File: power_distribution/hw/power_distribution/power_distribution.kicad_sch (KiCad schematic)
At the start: 52 parts, among them J1 XT30-M_Ver, J2 JST-PH_01x02, J3 JST-PH_01x02, J4 JST-PH_01x02, Q1 60Vds, U1 LMR51635XFDDCR, U2 AP63205WU-7, U3 AP63203WU-7

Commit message: First PCB draft
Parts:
- added C24: 0.1uF, Capacitor_SMD:C_0603_1608Metric_Pad1.08x0.95mm_HandSolder, symbol Device:C
- added D9: 3.3Vrwm, ESD5Z5.0T1G:SOD-523_0P9X1P3_ONS, symbol SMBJ51A-13-F:SMBJ51A-13-F
- added F5, F6: 0.5A 16V, 0ZCH0050FF2G:0ZCH_BEL, symbol Device:Polyfuse
- added J5: JST-PH_01x02, Connector_JST:JST_PH_S2B-PH-K_1x02_P2.00mm_Horizontal, symbol Connector_Generic:Conn_01x02
- added R7: 100k, Resistor_SMD:R_0603_1608Metric_Pad0.98x0.95mm_HandSolder, symbol Device:R_US
- C3: footprint Capacitor_SMD:CP_Elec_10x10 -> Capacitor_SMD:CP_Elec_8x10
- C5: footprint Capacitor_SMD:CP_Elec_10x10 -> Capacitor_SMD:CP_Elec_6.3x7.7
- C7: footprint Capacitor_SMD:CP_Elec_10x10 -> Capacitor_SMD:CP_Elec_5x5.3
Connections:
- net GND: now also C24.2, D9.2, J5.1 (Pin_1)
- net VBAT: now also R7.2; no longer U1.2 (EN)
- net at C8.1, D7.1, J4.2 (Pin_2): now also F5.1; no longer C7.1, D8.2 (A), F4.1
- new net: C24.1, D9.1, F6.1, J5.2 (Pin_2)
- new net: R7.1, U1.2 (EN)
- new net 3V3_SPLIT: C7.1, D8.2 (A), F4.1, F5.2, F6.2
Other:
- moved on the sheet: C1, C10, C11, C12, C13, C14, C15, C16, C17, C18, C19, C2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

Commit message: Add test points
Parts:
- added 12V: 12V, TestPoint:TestPoint_Pad_D1.0mm, symbol Connector:TestPoint
- added 3V3: 3V3, TestPoint:TestPoint_Pad_D1.0mm, symbol Connector:TestPoint
- added 5V: 5V, TestPoint:TestPoint_Pad_D1.0mm, symbol Connector:TestPoint
- added EN_12V: EN_12V, TestPoint:TestPoint_Pad_D1.0mm, symbol Connector:TestPoint
- added EN_3V3: EN_3V3, TestPoint:TestPoint_Pad_D1.0mm, symbol Connector:TestPoint
- added EN_5V: EN_5V, TestPoint:TestPoint_Pad_D1.0mm, symbol Connector:TestPoint
- added FB_12V: FB_12V, TestPoint:TestPoint_Pad_D1.0mm, symbol Connector:TestPoint
- added FB_3V3: FB_3V3, TestPoint:TestPoint_Pad_D1.0mm, symbol Connector:TestPoint
- added FB_5V: FB_5V, TestPoint:TestPoint_Pad_D1.0mm, symbol Connector:TestPoint
- added GND (x3): GND, TestPoint:TestPoint_Pad_D1.0mm, symbol Connector:TestPoint
- added SW_12V: SW_12V, TestPoint:TestPoint_Pad_D1.0mm, symbol Connector:TestPoint
- added SW_3V3: SW_3V3, TestPoint:TestPoint_Pad_D1.0mm, symbol Connector:TestPoint
- added SW_5V: SW_5V, TestPoint:TestPoint_Pad_D1.0mm, symbol Connector:TestPoint
- added VBAT: VBAT, TestPoint:TestPoint_Pad_D1.0mm, symbol Connector:TestPoint
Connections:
- net 12V_BUS: now also 12V.1, EN_5V.1
- net 3V3_BUS: now also 3V3.1, FB_3V3.1
- net 5V_BUS: now also 5V.1, EN_3V3.1, FB_5V.1
- net GND: now also GND.1, GND.1, GND.1
- net VBAT: now also VBAT.1
- net at R7.1, U1.2 (EN): now also EN_12V.1
- net at C17.2, L2.1, U2.5 (SW): now also SW_5V.1
- net at R5.2, R6.1, U1.1 (FB): now also FB_12V.1
- net at C13.2, L1.1, U1.5 (SW): now also SW_12V.1
- net at C21.2, L3.1, U3.5 (SW): now also SW_3V3.1

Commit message: Add mounting holes and refactor test points
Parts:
- added H1, H2, H3, H4: MountingHole_Pad, MountingHole:MountingHole_2.2mm_M2_Pad_Via, symbol Mechanical:MountingHole_Pad
- 12V1: renamed from 12V; footprint TestPoint:TestPoint_Pad_D1.0mm -> test_point_custom:TestPoint_Pad_D1.0mm
- 3V3, EN_3V3, FB_3V3, SW_3V3: footprint TestPoint:TestPoint_Pad_D1.0mm -> test_point_custom:TestPoint_Pad_D1.0mm
- 5V1: renamed from 5V; footprint TestPoint:TestPoint_Pad_D1.0mm -> test_point_custom:TestPoint_Pad_D1.0mm
- EN_12V1: renamed from EN_12V; footprint TestPoint:TestPoint_Pad_D1.0mm -> test_point_custom:TestPoint_Pad_D1.0mm
- EN_5V1: renamed from EN_5V; footprint TestPoint:TestPoint_Pad_D1.0mm -> test_point_custom:TestPoint_Pad_D1.0mm
- FB_12V1: renamed from FB_12V; footprint TestPoint:TestPoint_Pad_D1.0mm -> test_point_custom:TestPoint_Pad_D1.0mm
- FB_5V1: renamed from FB_5V; footprint TestPoint:TestPoint_Pad_D1.0mm -> test_point_custom:TestPoint_Pad_D1.0mm
- GND1, GND2, GND3: renamed from GND; footprint TestPoint:TestPoint_Pad_D1.0mm -> test_point_custom:TestPoint_Pad_D1.0mm
- SW_12V1: renamed from SW_12V; footprint TestPoint:TestPoint_Pad_D1.0mm -> test_point_custom:TestPoint_Pad_D1.0mm
- SW_5V1: renamed from SW_5V; footprint TestPoint:TestPoint_Pad_D1.0mm -> test_point_custom:TestPoint_Pad_D1.0mm
- VBAT1: renamed from VBAT; footprint TestPoint:TestPoint_Pad_D1.0mm -> test_point_custom:TestPoint_Pad_D1.0mm
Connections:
- no-connect marks 0 -> 4

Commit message: Finish finding last parts and 3D models
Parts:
- L1: footprint Inductor_SMD:L_10.4x10.4_H4.8 -> 7447714560:IND_1050P-WE-PD_WRE
- L2: footprint Inductor_SMD:L_7.3x7.3_H4.5 -> 7447779004:IND_7345R_WE-PD_WRE
- L3: footprint Inductor_SMD:L_6.3x6.3_H3 -> 74404052039:IND_WE-LQS_5020_WRE
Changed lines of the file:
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@@
 			)
 		)
-		(property "Footprint" "Inductor_SMD:L_7.3x7.3_H4.5"
+		(property "Footprint" "7447779004:IND_7345R_WE-PD_WRE"
 			(at 298.45 101.6 0)
 			(effects
@@
 			)
 		)
-		(property "Footprint" "Inductor_SMD:L_6.3x6.3_H3"
+		(property "Footprint" "74404052039:IND_WE-LQS_5020_WRE"
 			(at 298.45 165.1 0)
 			(effects
@@
 			)
 		)
-		(property "Footprint" "Inductor_SMD:L_10.4x10.4_H4.8"
+		(property "Footprint" "7447714560:IND_1050P-WE-PD_WRE"
 			(at 298.45 38.1 0)
 			(effects
@@
 			)
 		)
-		(property "Datasheet" "~"
+		(property "Datasheet" ""
 			(at 298.45 38.1 0)
 			(effects
@@
 			)
 		)
-		(property "Description" "Inductor"
+		(property "Description" ""
 			(at 298.45 38.1 0)
 			(effects

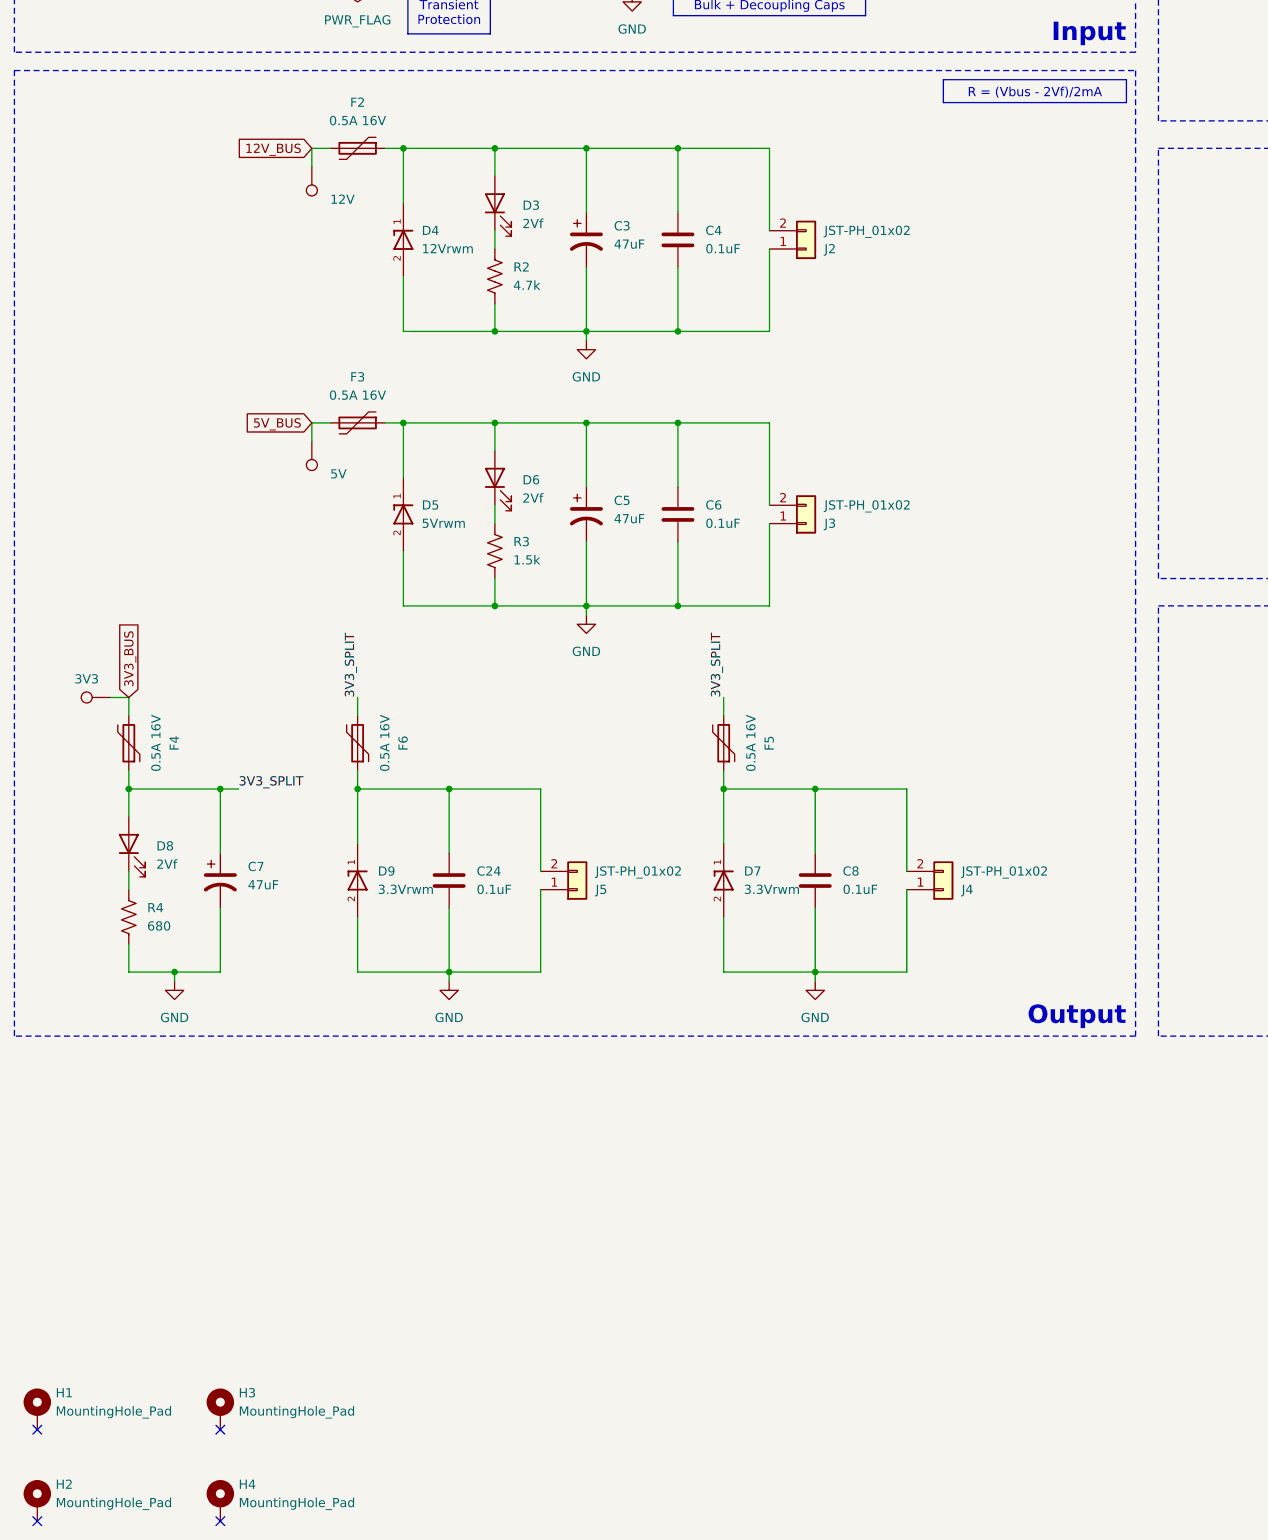
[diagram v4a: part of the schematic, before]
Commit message: Add sheet info
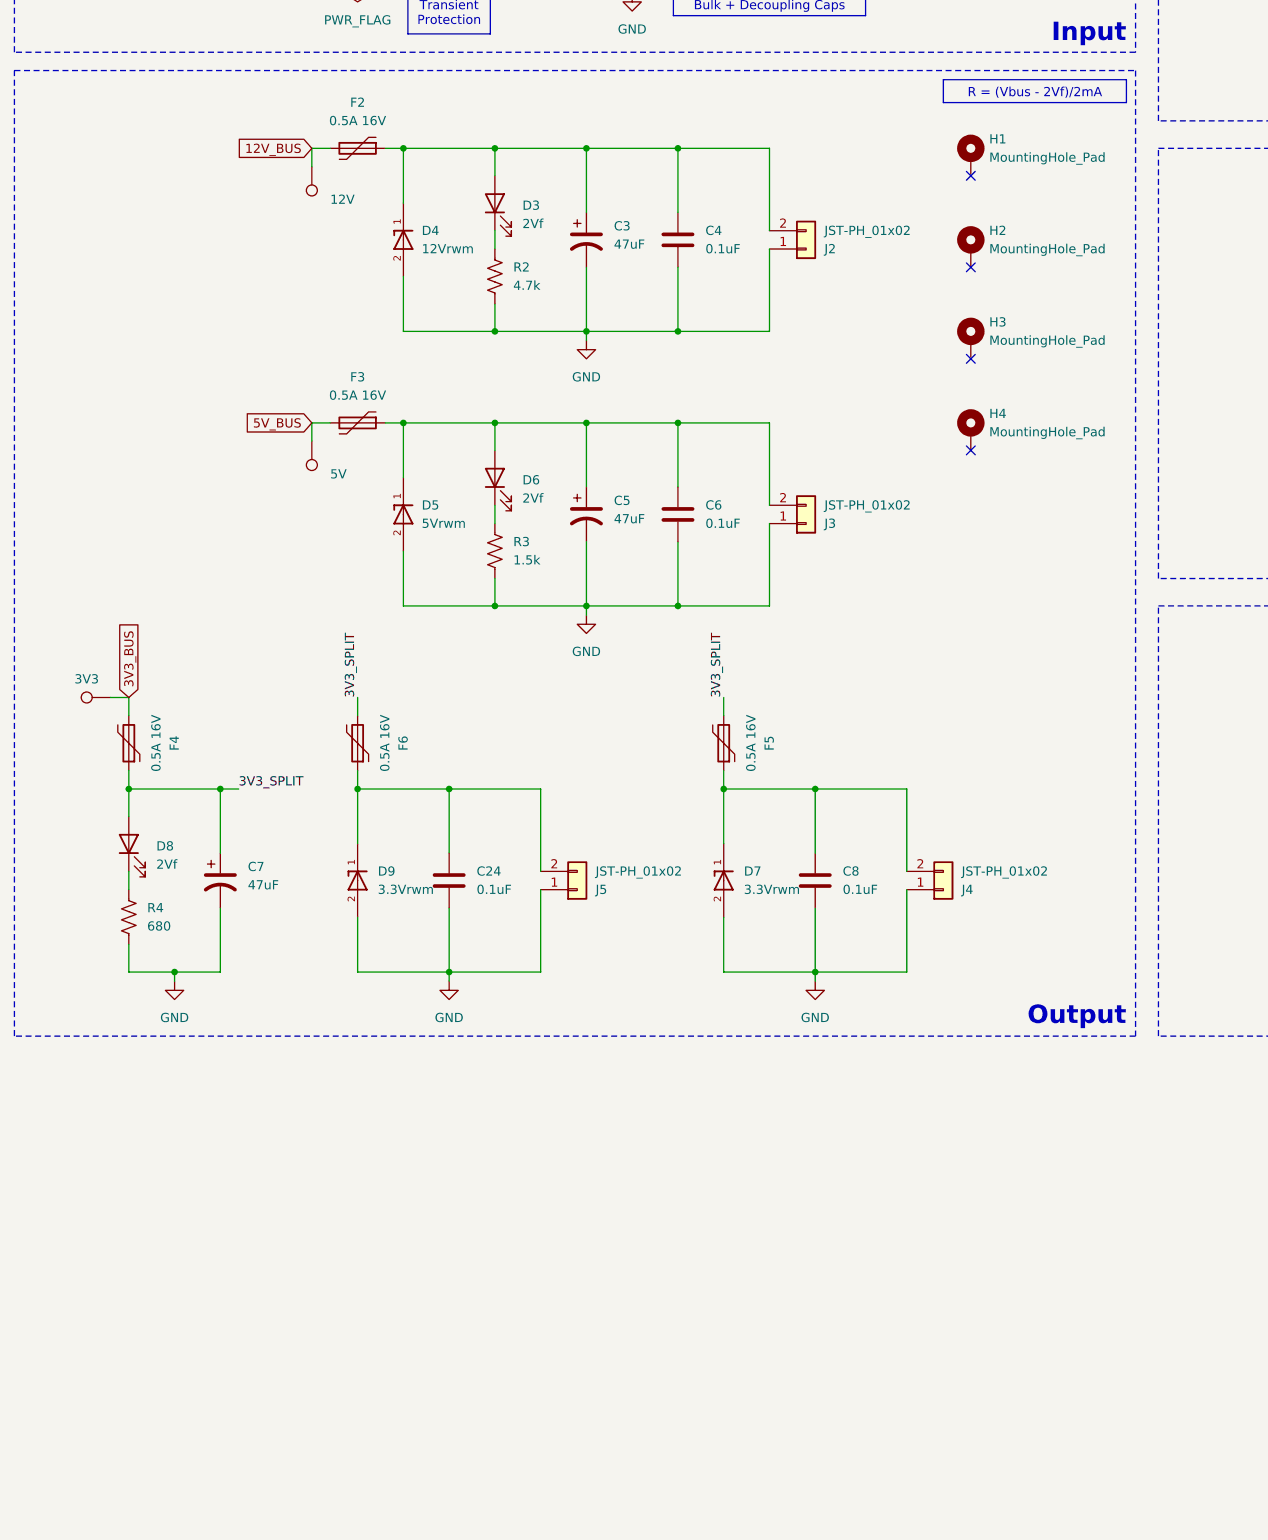
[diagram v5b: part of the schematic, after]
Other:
- company: Author: Leopoldo Mendoza -> Electrium Mobility
- moved on the sheet: H1, H2, H3, H4
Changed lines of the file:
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@@
 		(date "2025-10-05")
 		(rev "v1")
-		(company "Author: Leopoldo Mendoza")
+		(company "Electrium Mobility")
+		(comment 1 "Author: Leopoldo Mendoza")
 	)
 	(rectangle
@@
 	)
 	(no_connect
-		(at 50.8 264.16)
+		(at 154.94 115.57)
 	)
 	(no_connect
-		(at 25.4 276.86)
+		(at 154.94 102.87)
 	)
 	(no_connect
-		(at 25.4 264.16)
+		(at 154.94 90.17)
 	)
 	(no_connect
-		(at 50.8 276.86)
+		(at 154.94 128.27)
 	)
 	(wire
@@
 	(symbol
 		(lib_id "Mechanical:MountingHole_Pad")
-		(at 25.4 274.32 0)
+		(at 154.94 100.33 0)
 		(unit 1)
 		(exclude_from_sim no)
@@
 		(fields_autoplaced yes)
 		(property "Reference" "H2"
-			(at 27.94 271.7799 0)
+			(at 157.48 97.7899 0)
 			(effects
 				(font
@@
 		)
 		(property "Value" "MountingHole_Pad"
-			(at 27.94 274.3199 0)
+			(at 157.48 100.3299 0)
 			(effects
 				(font
@@
 		)
 		(property "Footprint" "MountingHole:MountingHole_2.2mm_M2_Pad_Via"
-			(at 25.4 274.32 0)
+			(at 154.94 100.33 0)
 			(effects
 				(font
@@
 		)
 		(property "Datasheet" "~"
-			(at 25.4 274.32 0)
+			(at 154.94 100.33 0)
 			(effects
 				(font
@@
 		)
 		(property "Description" "Mounting Hole with connection"
-			(at 25.4 274.32 0)
+			(at 154.94 100.33 0)
 			(effects
 				(font
@@
 	(symbol
 		(lib_id "Mechanical:MountingHole_Pad")
-		(at 50.8 261.62 0)
+		(at 154.94 113.03 0)
 		(unit 1)
 		(exclude_from_sim no)
@@
 		(fields_autoplaced yes)
 		(property "Reference" "H3"
-			(at 53.34 259.0799 0)
+			(at 157.48 110.4899 0)
 			(effects
 				(font
@@
 		)
 		(property "Value" "MountingHole_Pad"
-			(at 53.34 261.6199 0)
+			(at 157.48 113.0299 0)
 			(effects
 				(font
@@
 		)
 		(property "Footprint" "MountingHole:MountingHole_2.2mm_M2_Pad_Via"
-			(at 50.8 261.62 0)
+			(at 154.94 113.03 0)
 			(effects
 				(font
@@
 		)
 		(property "Datasheet" "~"
-			(at 50.8 261.62 0)
+			(at 154.94 113.03 0)
 			(effects
 				(font
@@
 		)
 		(property "Description" "Mounting Hole with connection"
-			(at 50.8 261.62 0)
+			(at 154.94 113.03 0)
 			(effects
 				(font
@@
 	(symbol
 		(lib_id "Mechanical:MountingHole_Pad")
-		(at 50.8 274.32 0)
+		(at 154.94 125.73 0)
 		(unit 1)
 		(exclude_from_sim no)
@@
 		(fields_autoplaced yes)
 		(property "Reference" "H4"
-			(at 53.34 271.7799 0)
+			(at 157.48 123.1899 0)
 			(effects
 				(font
@@
 		)
 		(property "Value" "MountingHole_Pad"
-			(at 53.34 274.3199 0)
+			(at 157.48 125.7299 0)
 			(effects
 				(font
@@
 		)
 		(property "Footprint" "MountingHole:MountingHole_2.2mm_M2_Pad_Via"
-			(at 50.8 274.32 0)
+			(at 154.94 125.73 0)
 			(effects
 				(font
@@
 		)
 		(property "Datasheet" "~"
-			(at 50.8 274.32 0)
+			(at 154.94 125.73 0)
 			(effects
 				(font
@@
 		)
 		(property "Description" "Mounting Hole with connection"
-			(at 50.8 274.32 0)
+			(at 154.94 125.73 0)
 			(effects
 				(font
@@
 	(symbol
 		(lib_id "Mechanical:MountingHole_Pad")
-		(at 25.4 261.62 0)
+		(at 154.94 87.63 0)
 		(unit 1)
 		(exclude_from_sim no)
@@
 		(dnp no)
 		(property "Reference" "H1"
-			(at 27.94 259.0799 0)
+			(at 157.48 85.0899 0)
 			(effects
 				(font
@@
 		)
 		(property "Value" "MountingHole_Pad"
-			(at 27.94 261.6199 0)
+			(at 157.48 87.6299 0)
 			(effects
 				(font
@@
 		)
 		(property "Footprint" "MountingHole:MountingHole_2.2mm_M2_Pad_Via"
-			(at 25.4 261.62 0)
+			(at 154.94 87.63 0)
 			(effects
 				(font
@@
 		)
 		(property "Datasheet" "~"
-			(at 25.4 261.62 0)
+			(at 154.94 87.63 0)
 			(effects
 				(font
@@
 		)
 		(property "Description" "Mounting Hole with connection"
-			(at 25.4 261.62 0)
+			(at 154.94 87.63 0)
 			(effects
 				(font

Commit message: Updated BOM. Ordered parts!
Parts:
- H1, H2, H3, H4: footprint MountingHole:MountingHole_2.2mm_M2_Pad_Via -> MountingHole:MountingHole_2.5mm_Pad_Via
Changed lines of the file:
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@@
 			)
 		)
-		(property "Footprint" "MountingHole:MountingHole_2.2mm_M2_Pad_Via"
+		(property "Footprint" "MountingHole:MountingHole_2.5mm_Pad_Via"
 			(at 154.94 100.33 0)
 			(effects
@@
 			)
 		)
-		(property "Datasheet" "~"
+		(property "Datasheet" ""
 			(at 154.94 100.33 0)
 			(effects
@@
 			)
 		)
-		(property "Description" "Mounting Hole with connection"
+		(property "Description" ""
 			(at 154.94 100.33 0)
 			(effects
@@
 			)
 		)
-		(property "Footprint" "MountingHole:MountingHole_2.2mm_M2_Pad_Via"
+		(property "Footprint" "MountingHole:MountingHole_2.5mm_Pad_Via"
 			(at 154.94 113.03 0)
 			(effects
@@
 			)
 		)
-		(property "Datasheet" "~"
+		(property "Datasheet" ""
 			(at 154.94 113.03 0)
 			(effects
@@
 			)
 		)
-		(property "Description" "Mounting Hole with connection"
+		(property "Description" ""
 			(at 154.94 113.03 0)
 			(effects
@@
 			)
 		)
-		(property "Footprint" "MountingHole:MountingHole_2.2mm_M2_Pad_Via"
+		(property "Footprint" "MountingHole:MountingHole_2.5mm_Pad_Via"
 			(at 154.94 125.73 0)
 			(effects
@@
 			)
 		)
-		(property "Datasheet" "~"
+		(property "Datasheet" ""
 			(at 154.94 125.73 0)
 			(effects
@@
 			)
 		)
-		(property "Description" "Mounting Hole with connection"
+		(property "Description" ""
 			(at 154.94 125.73 0)
 			(effects
@@
 			)
 		)
-		(property "Footprint" "MountingHole:MountingHole_2.2mm_M2_Pad_Via"
+		(property "Footprint" "MountingHole:MountingHole_2.5mm_Pad_Via"
 			(at 154.94 87.63 0)
 			(effects
@@
 			)
 		)
-		(property "Datasheet" "~"
+		(property "Datasheet" ""
 			(at 154.94 87.63 0)
 			(effects
@@
 			)
 		)
-		(property "Description" "Mounting Hole with connection"
+		(property "Description" ""
 			(at 154.94 87.63 0)
 			(effects
